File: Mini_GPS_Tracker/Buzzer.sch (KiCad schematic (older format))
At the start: 4 parts, among them Q1 2N3904

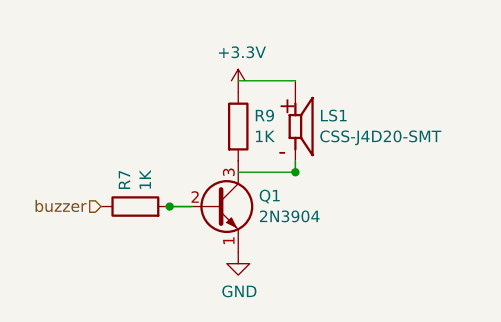
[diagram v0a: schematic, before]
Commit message: Add files via upload
More changes - USB, WiFi/BT, Buzzer, Siren-LED Flasher
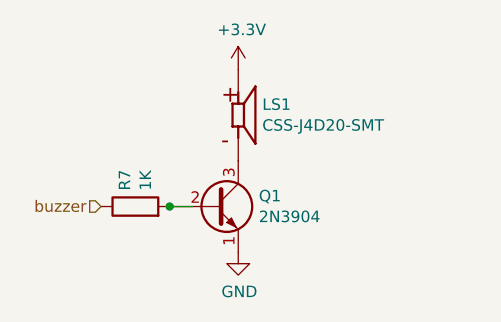
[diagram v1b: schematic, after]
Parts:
- removed R9: 1K, symbol Device:R
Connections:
- wire segments 4 -> 1
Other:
- moved on the sheet: LS1
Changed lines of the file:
@@
 $Descr A4 11693 8268
 encoding utf-8
-Sheet 11 13
+Sheet 1 13
 Title ""
 Date ""
@@
 Comment4 ""
 $EndDescr
-$Comp
-L Mini_GPS_Tracker-rescue:CSS-J4D20-SMT-Sparkfun_Artemis-Mini_GPS_Tracker-rescue LS?
-U 1 1 5EB2D6D8
-P 4200 3300
-AR Path="/5EB2D6D8" Ref="LS?"  Part="1"
-AR Path="/5EB2CC49/5EB2D6D8" Ref="LS1"  Part="1"
-F 0 "LS1" H 4305 3346 50  0000 L CNN
-F 1 "CSS-J4D20-SMT" H 4305 3255 50  0000 L CNN
-F 2 "Sparkfun-Artemis:CUI_CSS-J4D20-SMT" H 4200 3300 50  0001 L BNN
-F 3 "CUI" H 4200 3300 50  0001 L BNN
-F 4 "None" H 4200 3300 50  0001 L BNN "Field4"
-F 5 "CSS-J4D20-SMT" H 4200 3300 50  0001 L BNN "Field5"
-F 6 "Unavailable" H 4200 3300 50  0001 L BNN "Field6"
-F 7 "8.5 mm, 3.6 V, 90 dB, Surface Mount _SMT_, Magnetic Audio Transducer Buzzer" H 4200 3300 50  0001 L BNN "Field7"
-F 8 "None" H 4200 3300 50  0001 L BNN "Field8"
-	1    4200 3300
-	1    0    0    -1
-$EndComp
 $Comp
 L Device:R R?
@@
 	3750 3650 3650 3650
 $Comp
+L power:GND #PWR?
+U 1 1 5EB2D6ED
+P 3950 3850
+AR Path="/5EB2D6ED" Ref="#PWR?"  Part="1"
+AR Path="/5EB2CC49/5EB2D6ED" Ref="#PWR051"  Part="1"
+F 0 "#PWR051" H 3950 3600 50  0001 C CNN
+F 1 "GND" H 3955 3677 50  0000 C CNN
+F 2 "" H 3950 3850 50  0001 C CNN
+F 3 "" H 3950 3850 50  0001 C CNN
+	1    3950 3850
+	1    0    0    -1
+$EndComp
+Text HLabel 3350 3650 0    50   Input ~ 0
+buzzer
+$Comp
+L power:+3.3V #PWR?
+U 1 1 5EB2D6F9
+P 3950 3050
+AR Path="/5EB2D6F9" Ref="#PWR?"  Part="1"
+AR Path="/5EB2CC49/5EB2D6F9" Ref="#PWR050"  Part="1"
+F 0 "#PWR050" H 3950 2900 50  0001 C CNN
+F 1 "+3.3V" H 3965 3223 50  0000 C CNN
+F 2 "" H 3950 3050 50  0001 C CNN
+F 3 "" H 3950 3050 50  0001 C CNN
+	1    3950 3050
+	1    0    0    -1
+$EndComp
+Connection ~ 3650 3650
+$Comp
 L Transistor_BJT:2N3904 Q?
 U 1 1 5EB2D6E6
@@
 	1    0    0    -1
 $EndComp
-Connection ~ 3650 3650
 $Comp
-L power:GND #PWR?
-U 1 1 5EB2D6ED
-P 3950 3850
-AR Path="/5EB2D6ED" Ref="#PWR?"  Part="1"
-AR Path="/5EB2CC49/5EB2D6ED" Ref="#PWR051"  Part="1"
-F 0 "#PWR051" H 3950 3600 50  0001 C CNN
-F 1 "GND" H 3955 3677 50  0000 C CNN
-F 2 "" H 3950 3850 50  0001 C CNN
-F 3 "" H 3950 3850 50  0001 C CNN
-	1    3950 3850
+L Mini_GPS_Tracker-rescue:CSS-J4D20-SMT-Sparkfun_Artemis-Mini_GPS_Tracker-rescue LS?
+U 1 1 5EB2D6D8
+P 3950 3250
+AR Path="/5EB2D6D8" Ref="LS?"  Part="1"
+AR Path="/5EB2CC49/5EB2D6D8" Ref="LS1"  Part="1"
+F 0 "LS1" H 4055 3296 50  0000 L CNN
+F 1 "CSS-J4D20-SMT" H 4055 3205 50  0000 L CNN
+F 2 "Sparkfun-Artemis:CUI_CSS-J4D20-SMT" H 3950 3250 50  0001 L BNN
+F 3 "CUI" H 3950 3250 50  0001 L BNN
+F 4 "None" H 3950 3250 50  0001 L BNN "Field4"
+F 5 "CSS-J4D20-SMT" H 3950 3250 50  0001 L BNN "Field5"
+F 6 "Unavailable" H 3950 3250 50  0001 L BNN "Field6"
+F 7 "8.5 mm, 3.6 V, 90 dB, Surface Mount _SMT_, Magnetic Audio Transducer Buzzer" H 3950 3250 50  0001 L BNN "Field7"
+F 8 "None" H 3950 3250 50  0001 L BNN "Field8"
+	1    3950 3250
 	1    0    0    -1
 $EndComp
-$Comp
-L Device:R R?
-U 1 1 5EB2D6F3
-P 3950 3300
-AR Path="/5EB2D6F3" Ref="R?"  Part="1"
-AR Path="/5EB2CC49/5EB2D6F3" Ref="R9"  Part="1"
-F 0 "R9" H 4020 3346 50  0000 L CNN
-F 1 "1K" H 4020 3255 50  0000 L CNN
-F 2 "" V 3880 3300 50  0001 C CNN
-F 3 "~" H 3950 3300 50  0001 C CNN
-	1    3950 3300
-	1    0    0    -1
-$EndComp
-$Comp
-L power:+3.3V #PWR?
-U 1 1 5EB2D6F9
-P 3950 3150
-AR Path="/5EB2D6F9" Ref="#PWR?"  Part="1"
-AR Path="/5EB2CC49/5EB2D6F9" Ref="#PWR050"  Part="1"
-F 0 "#PWR050" H 3950 3000 50  0001 C CNN
-F 1 "+3.3V" H 3965 3323 50  0000 C CNN
-F 2 "" H 3950 3150 50  0001 C CNN
-F 3 "" H 3950 3150 50  0001 C CNN
-	1    3950 3150
-	1    0    0    -1
-$EndComp
-Wire Wire Line
-	3950 3100 4200 3100
-Wire Wire Line
-	3950 3500 4200 3500
-Wire Wire Line
-	4200 3450 4200 3500
-Connection ~ 4200 3500
-Text HLabel 3350 3650 0    50   Input ~ 0
-buzzer
 $EndSCHEMATC
